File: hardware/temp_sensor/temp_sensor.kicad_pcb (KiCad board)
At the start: 4 copper layers, 21.5 x 40 mm, 20 parts, among them J1 USB_A, Q1 Q_NPN_BEC, Q2 Q_NPN_BEC, U1 AZ1117-3.3, U2 SHT31-DIS, U3 ESP32-WROOM-32, U4 CH340C

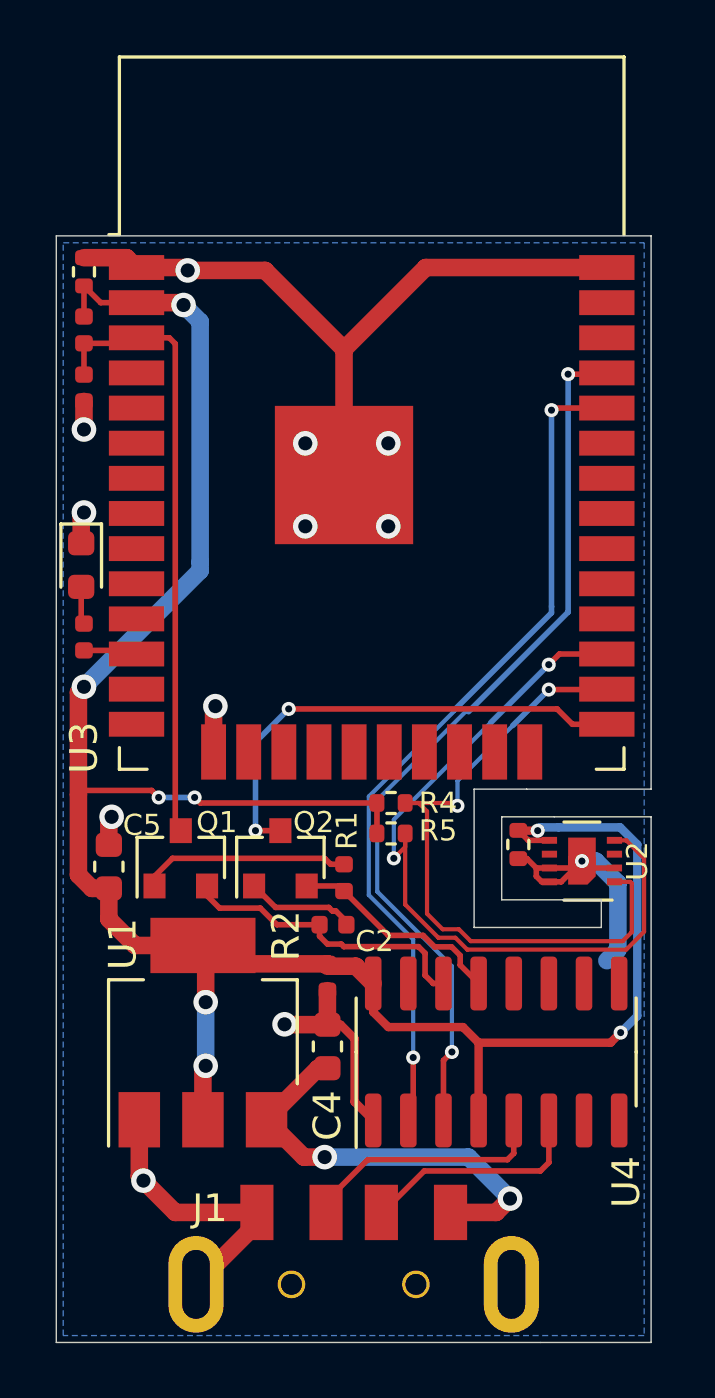
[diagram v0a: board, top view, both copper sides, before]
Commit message: Updated garden controller hardware to version 4
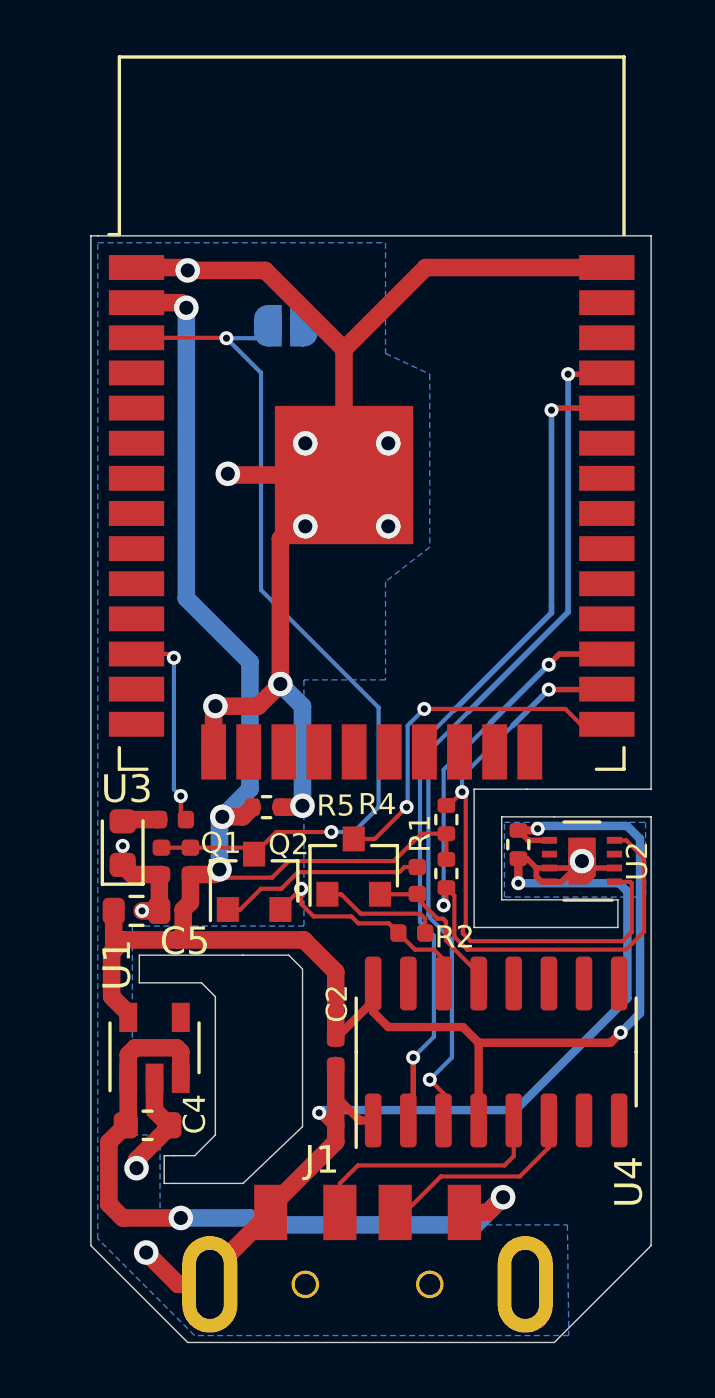
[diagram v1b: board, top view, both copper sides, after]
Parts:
- added JP1: SolderJumper_2_Open, Jumper:SolderJumper-2_P1.3mm_Open_RoundedPad1.0x1.5mm, B.Cu at (57.3, 44.8)
- C5: value 22uF -> 1uF
- U1: value AZ1117-3.3 -> AP2112K-3.3; footprint Package_TO_SOT_SMD:SOT-223-3_TabPin2 -> Package_TO_SOT_SMD:SOT-23-5
- moved C1 20.4 mm to (56.6, 62.1), turned to 0 degrees
- moved R3 19.6 mm to (53.9, 64.1), turned to 270 degrees
- moved C6 17.3 mm to (52.8, 64.1)
- moved D11 10.2 mm to (51.4, 63.5), turned to 90 degrees
- moved R12 7.33 mm to (53.2, 62.6), turned to 180 degrees
- moved C4 7.10 mm to (52.3, 73.7), turned to 0 degrees
- moved R2 2.87 mm to (61.9, 66.7)
- moved Q1 2.78 mm to (56.1, 64.8)
- moved C2 2.72 mm to (59.1, 71.0)
- moved Q2 2.67 mm to (59.8, 64.3)
- moved R1 2.65 mm to (62.0, 64.8)
- moved R5 2.47 mm to (63.1, 64.5), turned to 90 degrees
- moved R4 2.09 mm to (63.1, 62.6), turned to 270 degrees
- moved C5 1.89 mm to (51.9, 65.9), turned to 0 degrees
- moved U1 1.83 mm to (52.5, 70.8)
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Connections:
- U1 pad 1: GND -> VBUS
- U1 pad 2: +3V3 -> GND
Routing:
- net GND: track 68.2 -> 107.7 mm, vias 12 -> 16
- net /EN: track 22.3 -> 32.8 mm, vias 0 -> 2
- net VBUS: track 15.3 -> 25.3 mm
- net /LED1: track 1.95 -> 7.44 mm, vias 0 -> 2
- net /IO0: track 17.5 -> 13.0 mm
- net /SDA: track 24.6 -> 21.9 mm
- net +3V3: track 85.4 -> 82.9 mm, vias 8 -> 5
- net /USB_RTS: track 10.9 -> 8.50 mm, vias 0 -> 1
- net /SCL: track 28.8 -> 26.4 mm
- net /USB_DTR: track 7.88 -> 5.63 mm
- net /USB_RX: track 32.6 -> 31.3 mm
- net /USB_TX: track 31.2 -> 30.3 mm
- net /USB_DM: track 8.32 -> 7.50 mm
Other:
- board size 21.5 x 40 mm -> 20.2 x 40 mm
- board text added: "RESET"
- board text added: "Wifi Temp/Humidity Sensor (Rev3) Dubious Creations https://dubiouscreations.com"
- board text removed: "Wifi Temp/Humidity Sensor Dubious Creations https://dubiouscreations.com"
